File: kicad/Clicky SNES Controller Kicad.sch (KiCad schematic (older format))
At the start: 70 parts, among them P1 CONN_01X05, P10 CONN_01X02, P11 CONN_01X03, P12 CONN_01X03, P13 CONN_01X02, P14 CONN_01X02, P2 CONN_01X01, P3 CONN_01X05, P4 CONN_01X01, P5 CONN_01X01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

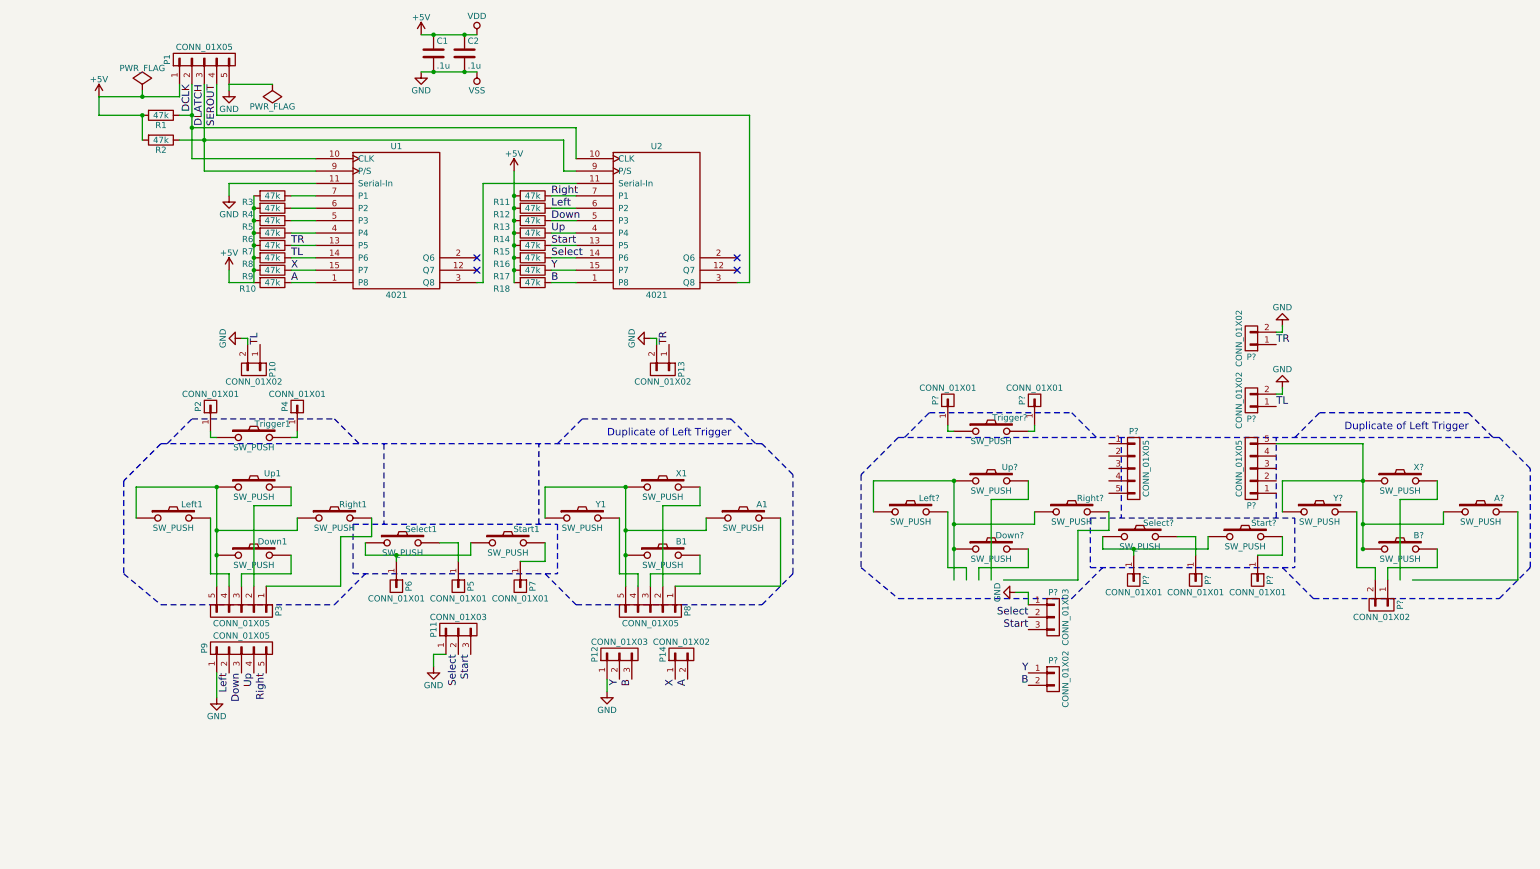
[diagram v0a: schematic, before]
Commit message: Schematic Rev 2 - Reduce connector count
-refactor the design to reduce the amount of board-to-board wires
-label board-to-board connectors
-add board-to-board wiring documentation
-split voltage domains between the two shift registers (creating 2 new
 parts in the project cache lib)
-move custom cmos4000 lib out of the project directory
-create new netlist
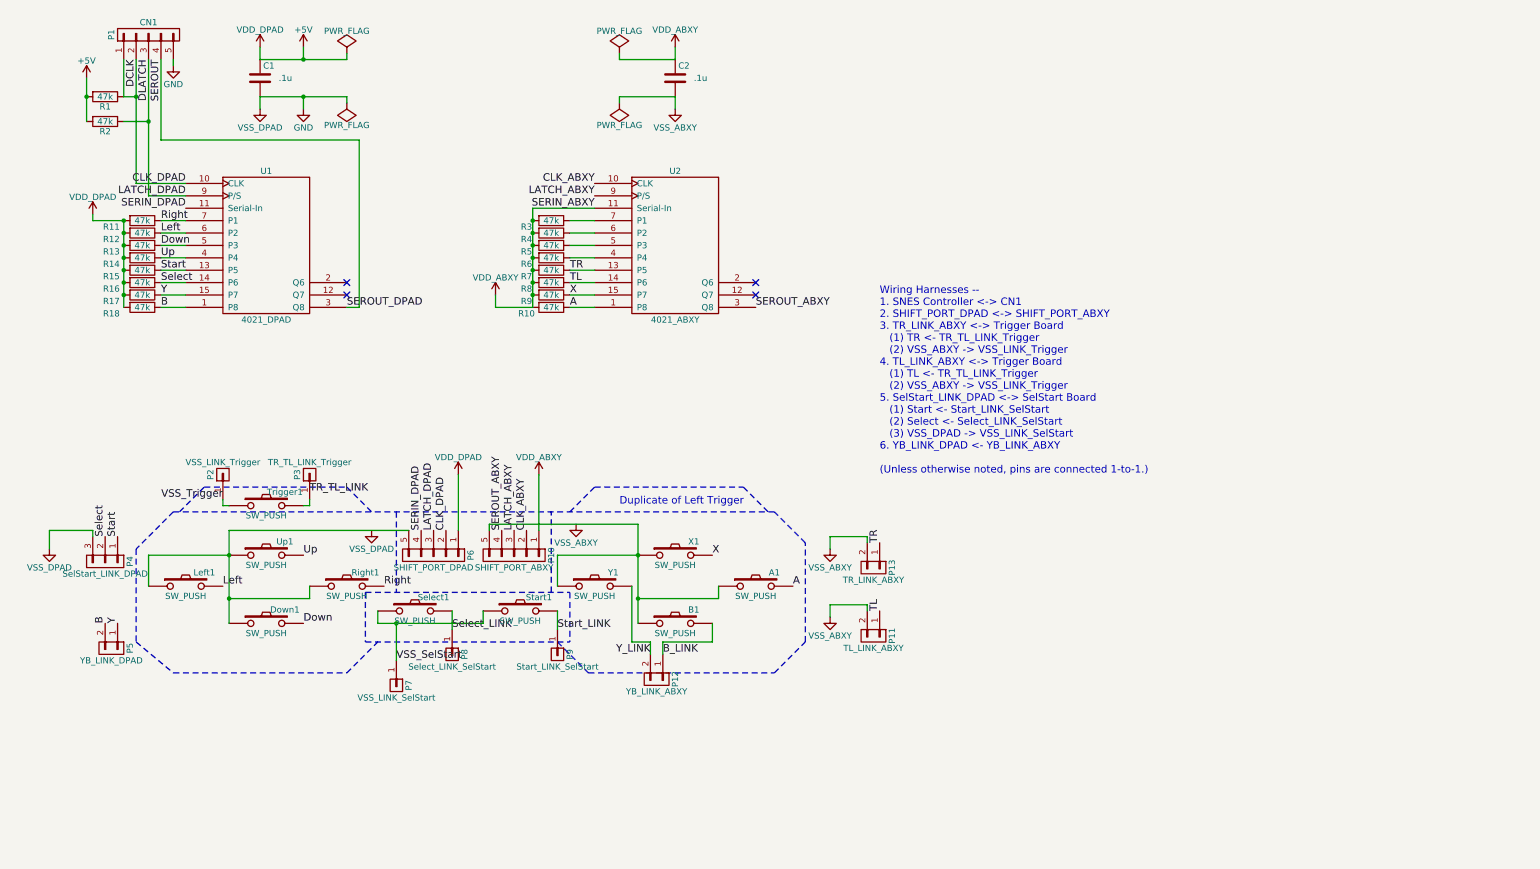
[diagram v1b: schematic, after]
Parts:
- removed A1, B1, Down1, Left1, Right1, Select1, Start1, Trigger1, Up1, X1, Y1: SW_PUSH, Buttons_Switches_SMD:SW_SPST_B3S-1000, symbol SW_PUSH
- removed P10, P13, P14: CONN_01X02, Wire_Pads:SolderWirePad_2x_0-8mmDrill, symbol CONN_01X02
- removed P11, P12: CONN_01X03, Wire_Pads:SolderWirePad_3x_0-8mmDrill, symbol CONN_01X03
- removed P2, P4, P5, P6, P7: CONN_01X01, Wire_Pads:SolderWirePad_single_0-8mmDrill, symbol CONN_01X01
- removed P3, P8, P9: CONN_01X05, Pin_Headers:Pin_Header_Straight_1x05_Pitch2.54mm, symbol CONN_01X05
- removed U1, U2: 4021, Housings_SOIC:SOIC-16_3.9x9.9mm_Pitch1.27mm, symbol 4021
- added U1: 4021_DPAD, symbol 4021_DPAD
- added U2: 4021_ABXY, symbol 4021_ABXY
- P1: value CONN_01X05 -> CN1
- P10: renamed from P?; value CONN_01X05 -> SHIFT_PORT_ABXY
- P11: renamed from P?; value CONN_01X02 -> TL_LINK_ABXY
- P12: renamed from P?; value CONN_01X02 -> YB_LINK_ABXY
- P13: renamed from P?; value CONN_01X02 -> TR_LINK_ABXY
- P2: renamed from P?; value CONN_01X01 -> VSS_LINK_Trigger
- P3: renamed from P?; value CONN_01X01 -> TR_TL_LINK_Trigger
- P4: renamed from P?; value CONN_01X03 -> SelStart_LINK_DPAD
- P5: renamed from P?; value CONN_01X02 -> YB_LINK_DPAD
- P6: renamed from P?; value CONN_01X05 -> SHIFT_PORT_DPAD
- P7: renamed from P?; value CONN_01X01 -> VSS_LINK_SelStart
- P8: renamed from P?; value CONN_01X01 -> Select_LINK_SelStart
- P9: renamed from P?; value CONN_01X01 -> Start_LINK_SelStart
- gave numbers to parts that had none: 11
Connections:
- net labels added: B_LINK, CLK_ABXY, CLK_DPAD, LATCH_ABXY, LATCH_DPAD, SERIN_ABXY, SERIN_DPAD, SEROUT_ABXY, SEROUT_DPAD, Select_LINK, Start_LINK, TR_TL_LINK, VDD_ABXY, VDD_DPAD, VSS_ABXY, VSS_DPAD, VSS_SelStart, VSS_Trigger, Y_LINK
- net labels removed: VDD, VSS
- wire segments 156 -> 90
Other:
- note added: "Wiring Harnesses --\n1. SNES Controller <-> CN1\n2. SHIFT_PORT_DPAD <-> SHIFT_PORT_ABXY\n3. TR_LINK_ABXY <-> Trigger Board\n (1) TR <- TR_TL_LINK_Trigger\n (2) VSS_ABXY -> VSS_LINK_Trigger\n4. TL_LINK_ABXY <-> Trigger Board\n (1) TL <- TR_TL_LINK_Trigger\n (2) VSS_ABXY -> VSS_LINK_Trigger\n5. SelStart_LINK_DPAD <-> SelStart Board\n (1) Start <- Start_LINK_SelStart\n (2) Select <- Select_LINK_SelS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"
- moved on the sheet: A1, B1, C1, C2, Down1, Left1, P1, P10, P11, P12, P13, P2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

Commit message: Add SOIC-16 package footprint to the shift registers
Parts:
- U1, U2: footprint (none) -> Housings_SOIC:SOIC-16_3.9x9.9mm_Pitch1.27mm
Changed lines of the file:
@@
 F 0 "U1" H 2550 3250 50  0000 C CNN
 F 1 "4021_DPAD" H 2550 2050 50  0000 C CNN
-F 2 "" H 2550 2650 60  0000 C CNN
+F 2 "Housings_SOIC:SOIC-16_3.9x9.9mm_Pitch1.27mm" H 2550 2650 60  0001 C CNN
 F 3 "" H 2550 2650 60  0000 C CNN
 	1    2550 2650
@@
 F 0 "U2" H 5850 3250 50  0000 C CNN
 F 1 "4021_ABXY" H 5850 2050 50  0000 C CNN
-F 2 "" H 5850 2650 60  0000 C CNN
+F 2 "Housings_SOIC:SOIC-16_3.9x9.9mm_Pitch1.27mm" H 5850 2650 60  0001 C CNN
 F 3 "" H 5850 2650 60  0000 C CNN
 	1    5850 2650

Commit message: Update footprint associations for the switches
Added custom footprints for all the switches.
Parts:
- A1, B1, X1, Y1: footprint Buttons_Switches_SMD:SW_SPST_B3S-1000 -> Extra_Buttons_Switches_SMD:SW_SPST_KSC7-G
- Down1, Left1, Right1, Up1: footprint Buttons_Switches_SMD:SW_SPST_B3S-1000 -> Extra_Buttons_Switches_SMD:SW_SPST_KSC2-G
- Select1, Start1: footprint Buttons_Switches_SMD:SW_SPST_B3S-1000 -> Extra_Buttons_Switches_SMD:SW_SPST_Plated_Pad_5.5mm
- Trigger1: footprint Buttons_Switches_SMD:SW_SPST_B3S-1000 -> Extra_Buttons_Switches_SMD:SW_SPST_KSC6-G
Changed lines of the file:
@@
 F 0 "B1" H 6000 5810 50  0000 C CNN
 F 1 "SW_PUSH" H 5850 5620 50  0000 C CNN
-F 2 "Buttons_Switches_SMD:SW_SPST_B3S-1000" H 5850 5700 50  0001 C CNN
+F 2 "Extra_Buttons_Switches_SMD:SW_SPST_KSC7-G" H 5850 5700 50  0001 C CNN
 F 3 "" H 5850 5700 50  0000 C CNN
 	1    5850 5700
@@
 F 0 "Y1" H 5350 5510 50  0000 C CNN
 F 1 "SW_PUSH" H 5200 5320 50  0000 C CNN
-F 2 "Buttons_Switches_SMD:SW_SPST_B3S-1000" H 5200 5400 50  0001 C CNN
+F 2 "Extra_Buttons_Switches_SMD:SW_SPST_KSC7-G" H 5200 5400 50  0001 C CNN
 F 3 "" H 5200 5400 50  0000 C CNN
 	1    5200 5400
@@
 F 0 "Start1" H 4750 5710 50  0000 C CNN
 F 1 "SW_PUSH" H 4600 5520 50  0000 C CNN
-F 2 "Buttons_Switches_SMD:SW_SPST_B3S-1000" H 4600 5600 50  0001 C CNN
+F 2 "Extra_Buttons_Switches_SMD:SW_SPST_Plated_Pad_5.5mm" H 4600 5600 50  0001 C CNN
 F 3 "" H 4600 5600 50  0000 C CNN
 	1    4600 5600
@@
 F 0 "Up1" H 2700 5260 50  0000 C CNN
 F 1 "SW_PUSH" H 2550 5070 50  0000 C CNN
-F 2 "Buttons_Switches_SMD:SW_SPST_B3S-1000" H 2550 5150 50  0001 C CNN
+F 2 "Extra_Buttons_Switches_SMD:SW_SPST_KSC2-G" H 2550 5150 50  0001 C CNN
 F 3 "" H 2550 5150 50  0000 C CNN
 	1    2550 5150
@@
 F 0 "Down1" H 2700 5810 50  0000 C CNN
 F 1 "SW_PUSH" H 2550 5620 50  0000 C CNN
-F 2 "Buttons_Switches_SMD:SW_SPST_B3S-1000" H 2550 5700 50  0001 C CNN
+F 2 "Extra_Buttons_Switches_SMD:SW_SPST_KSC2-G" H 2550 5700 50  0001 C CNN
 F 3 "" H 2550 5700 50  0000 C CNN
 	1    2550 5700
@@
 F 0 "Left1" H 2050 5510 50  0000 C CNN
 F 1 "SW_PUSH" H 1900 5320 50  0000 C CNN
-F 2 "Buttons_Switches_SMD:SW_SPST_B3S-1000" H 1900 5400 50  0001 C CNN
+F 2 "Extra_Buttons_Switches_SMD:SW_SPST_KSC2-G" H 1900 5400 50  0001 C CNN
 F 3 "" H 1900 5400 50  0000 C CNN
 	1    1900 5400
@@
 F 0 "Right1" H 3350 5510 50  0000 C CNN
 F 1 "SW_PUSH" H 3200 5320 50  0000 C CNN
-F 2 "Buttons_Switches_SMD:SW_SPST_B3S-1000" H 3200 5400 50  0001 C CNN
+F 2 "Extra_Buttons_Switches_SMD:SW_SPST_KSC2-G" H 3200 5400 50  0001 C CNN
 F 3 "" H 3200 5400 50  0000 C CNN
 	1    3200 5400
@@
 F 0 "A1" H 6650 5510 50  0000 C CNN
 F 1 "SW_PUSH" H 6500 5320 50  0000 C CNN
-F 2 "Buttons_Switches_SMD:SW_SPST_B3S-1000" H 6500 5400 50  0001 C CNN
+F 2 "Extra_Buttons_Switches_SMD:SW_SPST_KSC7-G" H 6500 5400 50  0001 C CNN
 F 3 "" H 6500 5400 50  0000 C CNN
 	1    6500 5400
@@
 F 0 "X1" H 6000 5260 50  0000 C CNN
 F 1 "SW_PUSH" H 5850 5070 50  0000 C CNN
-F 2 "Buttons_Switches_SMD:SW_SPST_B3S-1000" H 5850 5150 50  0001 C CNN
+F 2 "Extra_Buttons_Switches_SMD:SW_SPST_KSC7-G" H 5850 5150 50  0001 C CNN
 F 3 "" H 5850 5150 50  0000 C CNN
 	1    5850 5150
@@
 F 0 "Trigger1" H 2700 4860 50  0000 C CNN
 F 1 "SW_PUSH" H 2550 4670 50  0000 C CNN
-F 2 "Buttons_Switches_SMD:SW_SPST_B3S-1000" H 2550 4750 50  0001 C CNN
+F 2 "Extra_Buttons_Switches_SMD:SW_SPST_KSC6-G" H 2550 4750 50  0001 C CNN
 F 3 "" H 2550 4750 50  0000 C CNN
 	1    2550 4750
@@
 F 0 "Select1" H 3900 5710 50  0000 C CNN
 F 1 "SW_PUSH" H 3750 5520 50  0000 C CNN
-F 2 "Buttons_Switches_SMD:SW_SPST_B3S-1000" H 3750 5600 50  0001 C CNN
+F 2 "Extra_Buttons_Switches_SMD:SW_SPST_Plated_Pad_5.5mm" H 3750 5600 50  0001 C CNN
 F 3 "" H 3750 5600 50  0000 C CNN
 	1    3750 5600

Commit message: SCH/NET: Attempt to fix issue with VDD/VSS labels on headers
CN1 pin 1 was routed incorrectly and not labeled as VDD.
Some of the other connectors don't have proper association with local
VDD/VSS, nor do U1 and U2.
This change mostly fixes it, but U1 is still showing raw VDD/VSS
instead of the board-local VDD/VSS.
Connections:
- net +5V: now also P1.1 (P1)
- net CLK_DPAD: no longer P1.1 (P1)
- net GND: now also Down1.1, Left1.1, P6.5 (P5), Right1.1, Up1.1
- net VSS_ABXY: now also A1.1, B1.1, P10.5 (P5), X1.1, Y1.1
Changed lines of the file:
@@
 	1800 1150 1800 1200
-Wire Wire Line
-	1400 1150 1400 1450
 Wire Wire Line
 	4700 2350 5200 2350
@@
 Wire Wire Line
 	5400 1150 5400 1100
+Wire Wire Line
+	1400 1150 1400 1350
+Wire Wire Line
+	1400 1350 1100 1350
+Connection ~ 1100 1350
+Text Label 4750 4950 1    60   ~ 0
+VDD_ABXY
+Text Label 4350 4950 1    60   ~ 0
+VSS_ABXY
+Text Label 4100 4950 1    60   ~ 0
+VDD_DPAD
+Text Label 3700 4950 1    60   ~ 0
+VSS_DPAD
 $EndSCHEMATC

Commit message: Schematic Rev 3 - Rework board-to-board jumpers
Decided to go with 3 full size boards to fill the mechanical space in
the controller instead of using the 3rd board as a spare.
This allows to move CN1 and both ICs onto the center board, which now
has plenty of space.
This solves several problems working around plastic ridges behind the
boards where I wanted to place components and reduces the number of
board-to-board jumpers needed.
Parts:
- removed P10: SHIFT_PORT_ABXY, Pin_Headers:Pin_Header_Straight_1x05_Pitch2.54mm, symbol CONN_01X05
- removed P12: YB_LINK_ABXY, Wire_Pads:SolderWirePad_2x_0-8mmDrill, symbol CONN_01X02
- removed P4: SelStart_LINK_DPAD, Wire_Pads:SolderWirePad_3x_0-8mmDrill, symbol CONN_01X03
- removed P5: YB_LINK_DPAD, Wire_Pads:SolderWirePad_2x_0-8mmDrill, symbol CONN_01X02
- removed P7: VSS_LINK_SelStart, Wire_Pads:SolderWirePad_single_0-8mmDrill, symbol CONN_01X01
- removed P8: Select_LINK_SelStart, Wire_Pads:SolderWirePad_single_0-8mmDrill, symbol CONN_01X01
- removed P9: Start_LINK_SelStart, Wire_Pads:SolderWirePad_single_0-8mmDrill, symbol CONN_01X01
- removed R3, R4, R5: 47k, Resistors_SMD:R_1206_HandSoldering, symbol R
- added P4: DPAD_IN, Pin_Headers:Pin_Header_Straight_1x05_Pitch1.27mm, symbol CONN_01X05
- P11: value TL_LINK_ABXY -> TL_IN; footprint Wire_Pads:SolderWirePad_2x_0-8mmDrill -> Pin_Headers:Pin_Header_Straight_1x02_Pitch1.27mm
- P13: value TR_LINK_ABXY -> TR_IN; footprint Wire_Pads:SolderWirePad_2x_0-8mmDrill -> Pin_Headers:Pin_Header_Straight_1x02_Pitch1.27mm
- P2: value VSS_LINK_Trigger -> VSS_Trigger; footprint Wire_Pads:SolderWirePad_single_0-8mmDrill -> Pin_Headers:Pin_Header_Straight_1x01_Pitch1.27mm
- P3: value TR_TL_LINK_Trigger -> TR_TL_OUT; footprint Wire_Pads:SolderWirePad_single_0-8mmDrill -> Pin_Headers:Pin_Header_Straight_1x01_Pitch1.27mm
- P6: value SHIFT_PORT_DPAD -> ABXY_IN; footprint Pin_Headers:Pin_Header_Straight_1x05_Pitch2.54mm -> Pin_Headers:Pin_Header_Straight_1x05_Pitch1.27mm
- U1: value 4021_DPAD -> 4021; symbol 4021_DPAD -> 4021
- U2: value 4021_ABXY -> 4021; symbol 4021_ABXY -> 4021
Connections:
- net Down is gone; now on net B_switch: Down1.2, R13.1, U1.5 (P3)
- net LATCH_ABXY is gone; now on net DLATCH: U2.9 (P/S)
- net SEROUT_ABXY is gone; now on an unnamed net: U2.3 (Q8)
- net Select_LINK is gone; now on net Select: Select1.2
- net Start_LINK is gone; now on net Start: Start1.2
- net VDD_ABXY is gone; now on net +5V: C2.1, R10.2, R6.2, R7.2, R8.2, R9.2, U2.11 (Serial-In), U2.16 (VDD)
- net VSS_SelStart is gone; now on net GND: Select1.1, Start1.1
- net Y_LINK is gone; now on net Right: Y1.2
- net +5V: now also U2.5 (P3), U2.6 (P2), U2.7 (P1); no longer P6.1 (P1)
- net A: now also P6.2 (P2); no longer A1.2
- net B: now also P6.3 (P3)
- net DLATCH: no longer P6.3 (P3)
- net GND: now also A1.1, B1.1, C2.2, P11.1 (P1), P13.1 (P1), P6.1 (P1), U2.8 (VSS), X1.1, Y1.1, P4.1 (P1); no longer P6.5 (P5)
- net Left: now also X1.2, P4.4 (P4)
- net Right: now also P4.5 (P5)
- net TL: now also P11.2 (P2); no longer P11.1 (P1)
- net TR: now also P13.2 (P2); no longer P13.1 (P1)
- net X: now also P6.4 (P4); no longer X1.2
- net Y: now also P6.5 (P5)
- net B_LINK renamed B_switch
- net B_switch: now also P4.3 (P3)
- net CLK_ABXY renamed DCLK
- net DCLK: now also P1.2 (P2), R1.1, U1.10 (CLK)
- removed net CLK_DPAD: P1.2 (P2), P6.2 (P2), R1.1, U1.10 (CLK)
- net SERIN_DPAD: no longer names the net of U1.11 (Serial-In)
- net SERIN_DPAD: no longer P6.4 (P4)
- net Up renamed A_switch
- net A_switch: now also A1.2, P4.2 (P2)
- removed net VSS_ABXY: A1.1, B1.1, C2.2, P11.2 (P2), P13.2 (P2), U2.8 (VSS_ABXY), X1.1, Y1.1
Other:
- note added: "ABXY Board"
- note added: "DPAD Board"
- note added: "Keep near U1"
- note added: "Keep near U2"
- note added: "Main Board"
- note added: "Wiring Harnesses --\n1. SNES Controller <-> CN1\n2. DPAD_IN (DPAD Board) <-> DPAD_IN (Main Board)\n3. DPAD_IN (ABXY Board) <-> ABXY_IN (Main Board)\n3. TR_IN <-> Trigger Board\n (1) TR <- TR_TL_switch\n (2) GND -> VSS_Trigger\n4. TL_IN <-> Trigger Board\n (1) TL <- TR_TL_switch\n (2) GND -> VSS_Trigger\n\n(Unless otherwise noted, pins are connected 1-to-1.)"
- note removed: "Wiring Harnesses --\n1. SNES Controller <-> CN1\n2. SHIFT_PORT_DPAD <-> SHIFT_PORT_ABXY\n3. TR_LINK_ABXY <-> Trigger Board\n (1) TR <- TR_TL_LINK_Trigger\n (2) VSS_ABXY -> VSS_LINK_Trigger\n4. TL_LINK_ABXY <-> Trigger Board\n (1) TL <- TR_TL_LINK_Trigger\n (2) VSS_ABXY -> VSS_LINK_Trigger\n5. SelStart_LINK_DPAD <-> SelStart Board\n (1) Start <- Start_LINK_SelStart\n (2) Select <- Select_LINK_SelS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"
- moved on the sheet: A1, B1, C1, Down1, Left1, P11, P13, P2, P3, Right1, Select1, Start1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

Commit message: Change footprint for trigger connectors
Change these to use .1" headers in case I want to add connectors
later so that I can swap the trigger boards.
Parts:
- P11, P13: footprint Pin_Headers:Pin_Header_Straight_1x02_Pitch1.27mm -> Pin_Headers:Pin_Header_Angled_1x02_Pitch2.54mm
- P2, P3: footprint Pin_Headers:Pin_Header_Straight_1x01_Pitch1.27mm -> Pin_Headers:Pin_Header_Straight_1x01_Pitch2.54mm
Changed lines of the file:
@@
 F 0 "P2" H 1750 5450 50  0000 C CNN
 F 1 "VSS_Trigger" V 1850 5350 50  0000 C CNN
-F 2 "Pin_Headers:Pin_Header_Straight_1x01_Pitch1.27mm" H 1750 5350 50  0001 C CNN
+F 2 "Pin_Headers:Pin_Header_Straight_1x01_Pitch2.54mm" H 1750 5350 50  0001 C CNN
 F 3 "" H 1750 5350 50  0000 C CNN
 	1    1750 5350
@@
 F 0 "P3" H 2450 5450 50  0000 C CNN
 F 1 "TR_TL_OUT" V 2550 5350 50  0000 C CNN
-F 2 "Pin_Headers:Pin_Header_Straight_1x01_Pitch1.27mm" H 2450 5350 50  0001 C CNN
+F 2 "Pin_Headers:Pin_Header_Straight_1x01_Pitch2.54mm" H 2450 5350 50  0001 C CNN
 F 3 "" H 2450 5350 50  0000 C CNN
 	1    2450 5350
@@
 F 0 "P13" H 3600 5850 50  0000 C CNN
 F 1 "TR_IN" V 3700 5700 50  0000 C CNN
-F 2 "Pin_Headers:Pin_Header_Straight_1x02_Pitch1.27mm" H 3600 5700 50  0001 C CNN
+F 2 "Pin_Headers:Pin_Header_Angled_1x02_Pitch2.54mm" H 3600 5700 50  0001 C CNN
 F 3 "" H 3600 5700 50  0000 C CNN
 	1    3600 5700
@@
 F 0 "P11" H 3300 5850 50  0000 C CNN
 F 1 "TL_IN" V 3400 5700 50  0000 C CNN
-F 2 "Pin_Headers:Pin_Header_Straight_1x02_Pitch1.27mm" H 3300 5700 50  0001 C CNN
+F 2 "Pin_Headers:Pin_Header_Angled_1x02_Pitch2.54mm" H 3300 5700 50  0001 C CNN
 F 3 "" H 3300 5700 50  0000 C CNN
 	1    3300 5700

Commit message: SCH/NET: Remove extra pullup, Rename CN1 PCB: Imported new netlist, Arranged resistors in order
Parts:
- removed R6: 47k, Resistors_SMD:R_1206_HandSoldering, symbol R
- renumbered P1 to CN1
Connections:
- net +5V: now also U2.4 (P4)
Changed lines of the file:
@@
 $EndDescr
 $Comp
-L CONN_01X05 P1
+L CONN_01X05 CN1
 U 1 1 58A907FB
 P 1600 950
-F 0 "P1" H 1600 1250 50  0000 C CNN
+F 0 "CN1" H 1600 1250 50  0000 C CNN
 F 1 "CN1" V 1700 950 50  0000 C CNN
 F 2 "Pin_Headers:Pin_Header_Angled_1x05_Pitch2.54mm" H 1600 950 50  0001 C CNN
@@
 F 3 "" H 1250 1650 50  0000 C CNN
 	1    1250 1650
-	0    1    1    0
-$EndComp
-$Comp
-L R R6
-U 1 1 58A917AE
-P 4850 2750
-F 0 "R6" V 4900 2550 50  0000 C CNN
-F 1 "47k" V 4850 2750 50  0000 C CNN
-F 2 "Resistors_SMD:R_1206_HandSoldering" V 4780 2750 50  0001 C CNN
-F 3 "" H 4850 2750 50  0000 C CNN
-	1    4850 2750
 	0    1    1    0
 $EndComp
@@
 	5000 2850 5200 2850
 Wire Wire Line
-	5000 2750 5200 2750
+	4700 2750 5200 2750
 Wire Wire Line
 	4700 2650 5200 2650
@@
 Connection ~ 5100 6550
 Wire Wire Line
-	5100 6000 5100 6850
+	5100 6850 5100 6000
 Wire Wire Line
 	6350 6250 6350 7200
@@
 	5700 6150 5400 6150
 Wire Wire Line
-	5400 6150 5400 7100
+	5400 7100 5400 6150
 Wire Wire Line
 	2400 6000 2750 6000
@@
 	5050 6400 4650 6400
 Wire Wire Line
-	4650 6400 4650 7050
+	4650 7050 4650 6400
 Wire Wire Line
 	1750 7100 1750 6250
 Connection ~ 3600 7050
 Wire Wire Line
-	4650 7050 3050 7050
+	3050 7050 4650 7050
 Wire Wire Line
 	3600 7050 3600 7250
@@
 	6350 7200 3900 7200
 Wire Wire Line
-	5100 6850 1800 6850
+	1800 6850 5100 6850
 Wire Wire Line
 	2750 6900 3900 6900
@@
 	2400 6950 3800 6950
 Wire Wire Line
-	5400 7100 1750 7100
+	1750 7100 5400 7100
 Text Notes 3500 6800 0    60   ~ 0
 Main Board
